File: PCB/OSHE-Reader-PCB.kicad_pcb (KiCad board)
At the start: 2 copper layers, 80 x 100 mm, 76 parts, among them J1 UART, J2 112L-TDA0, J3 JTAG, J5 boot_select, Q1 Si1308EDL, Q2 BSS138, Q3 BSS138, U1 74LVC1G04, U2 TPS923610DRLR, U3 TLV75533PDBV, U4 ESP32-S3-WROOM-1

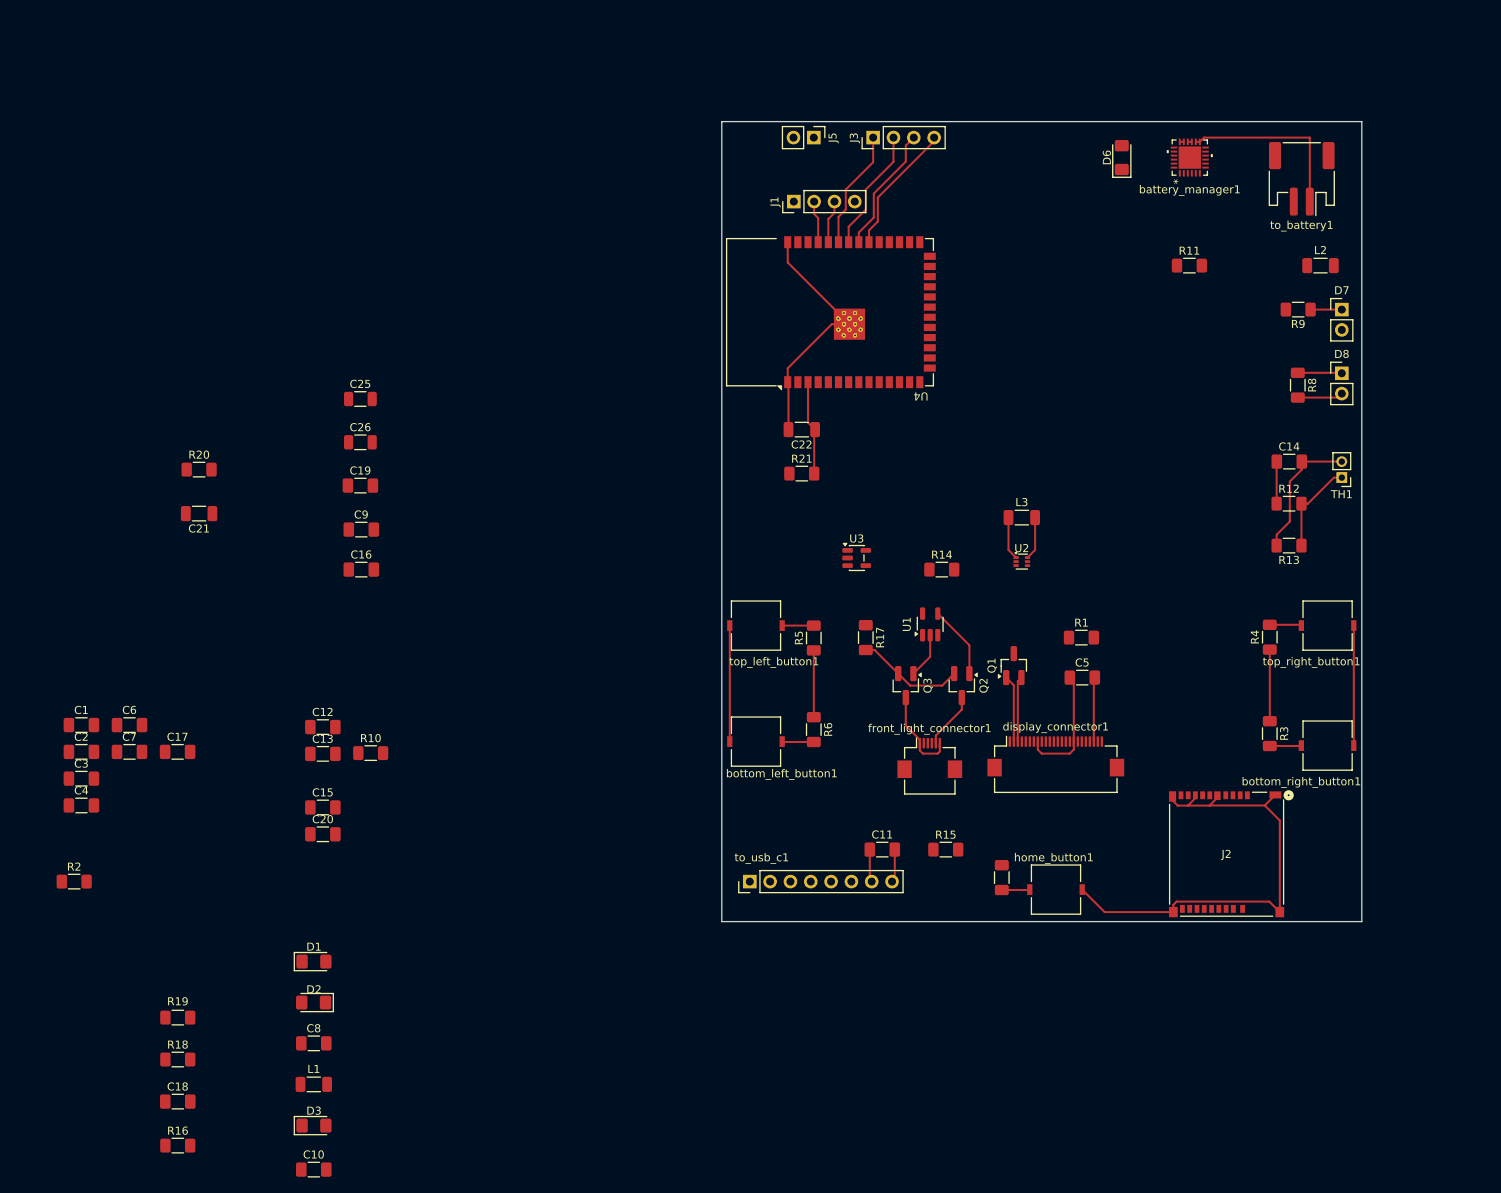
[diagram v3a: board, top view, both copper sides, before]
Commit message: Routed Board
Board is mostly routed except for the left buttons and center button in case they need to get moved. Looked through DRC for a first pass and got most of the errors I think but would appreciate a second set of eyes.
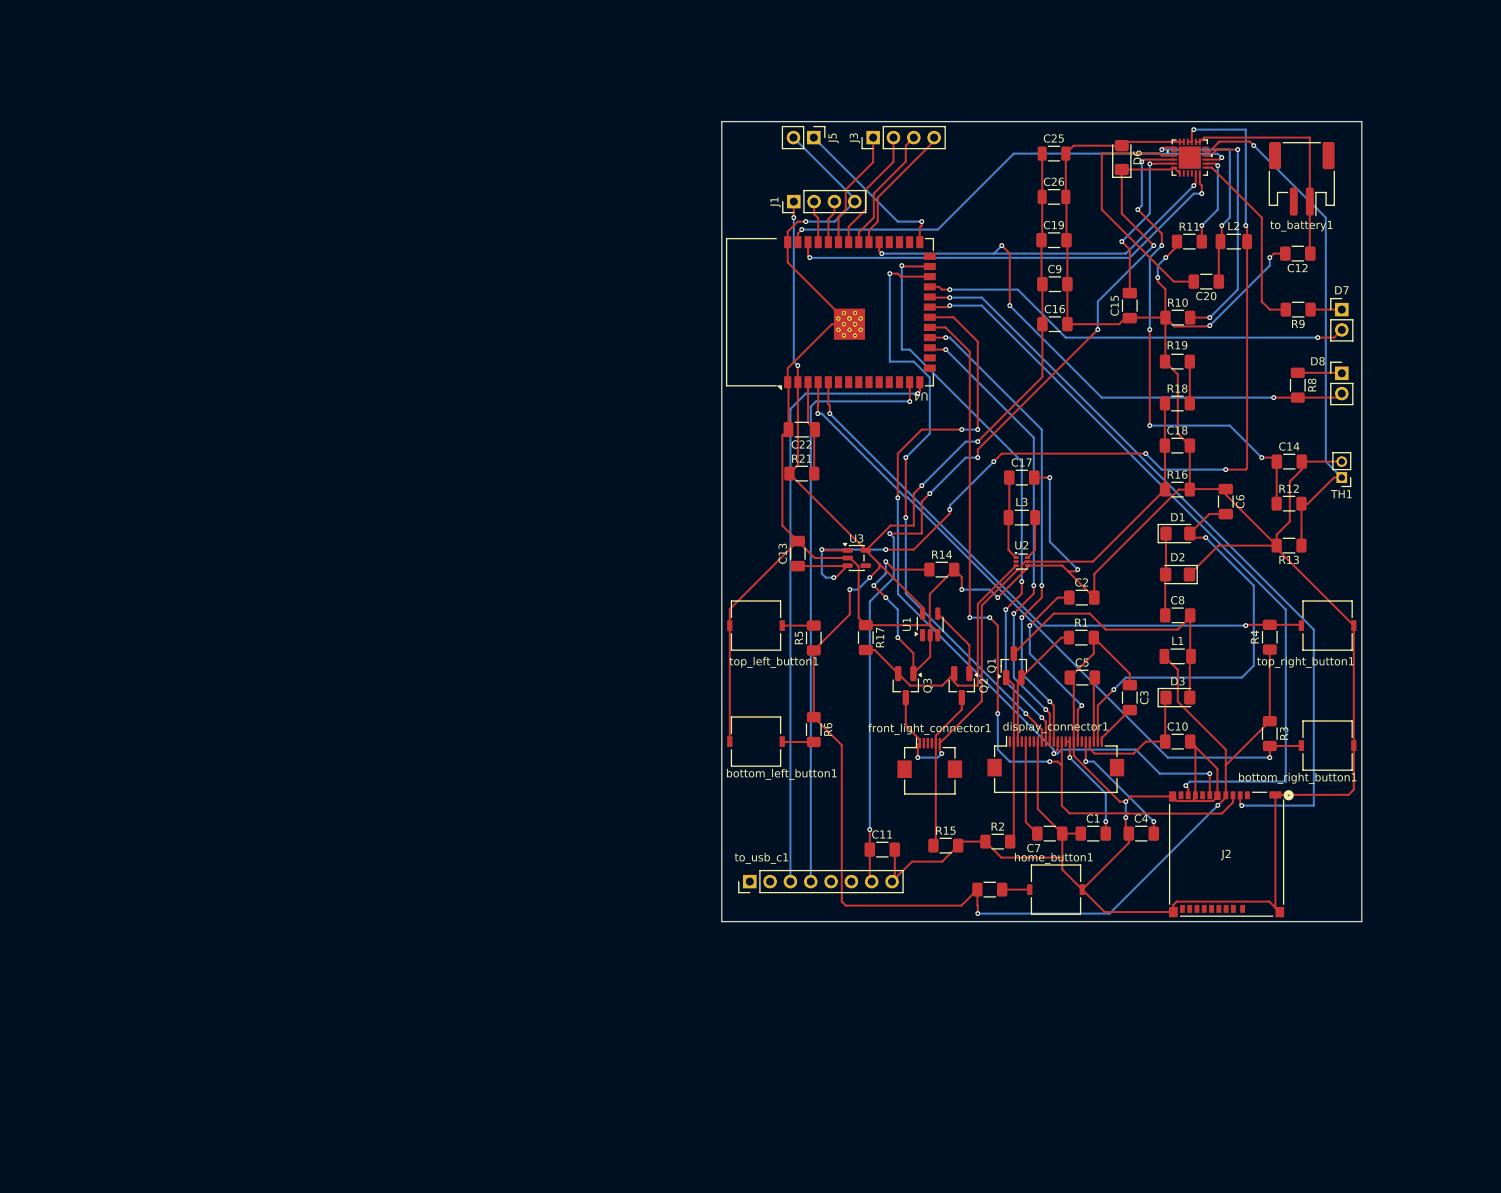
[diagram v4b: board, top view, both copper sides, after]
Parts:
- removed C21: 1uF, Inductor_SMD:L_1206_3216Metric_Pad1.22x1.90mm_HandSolder
- removed R20: 10k, Resistor_SMD:R_1206_3216Metric_Pad1.30x1.75mm_HandSolder
- moved C18 149.5 mm to (170.4, 89.0)
- moved R16 149.5 mm to (170.4, 94.5)
- moved R18 149.5 mm to (170.4, 83.7)
- moved R19 149.5 mm to (170.4, 78.5)
- moved C6 139.9 mm to (176.5, 96.0), turned to -90 degrees
- moved C12 135.5 mm to (185.5, 65.0), turned to 180 degrees
- moved C4 132.5 mm to (165.9, 137.5)
- moved C3 131.4 mm to (164.5, 120.5), turned to -90 degrees
- moved C20 130.3 mm to (174.1, 68.5), turned to 180 degrees
- moved C1 127.2 mm to (159.9, 137.5)
- moved C2 126.5 mm to (158.5, 108.0)
- moved C10 120.5 mm to (170.5, 126.0)
- moved C8 120.5 mm to (170.5, 110.2)
- moved D1 120.5 mm to (170.5, 100.0)
- moved D2 120.5 mm to (170.5, 105.1)
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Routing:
- net GND: track 156.3 -> 551.1 mm, vias 0 -> 11
- net +3V3: track 17.3 -> 263.7 mm, vias 0 -> 8
- net /Battery Charger/SYS: track 0.50 -> 127.2 mm, vias 0 -> 9
- net /VBUS: track 4.10 -> 116.8 mm, vias 0 -> 6
- net /SCL: track 0.00 -> 100.4 mm, vias 0 -> 5
- net /COPI: track 0.00 -> 99.0 mm, vias 0 -> 4
- net /SD_CS: track 0.00 -> 97.6 mm, vias 0 -> 2
- net /CIPO: track 0.00 -> 95.9 mm, vias 0 -> 2
- net /STAT: track 5.71 -> 101.5 mm, vias 0 -> 5
- net /BR_button: track 3.97 -> 83.7 mm, vias 0 -> 2
- net /D+: track 0.00 -> 77.3 mm, vias 0 -> 1
- net /BUSY: track 0.00 -> 75.8 mm, vias 0 -> 4
- net /D-: track 0.00 -> 74.5 mm, vias 0 -> 1
- net /RES_SCR: track 0.00 -> 72.7 mm, vias 0 -> 4
- net /TR_button: track 3.99 -> 74.0 mm, vias 0 -> 2
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
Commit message: pcb
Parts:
- moved C1 49.4 mm to (113.1, 153.0)
- moved C4 49.4 mm to (119.1, 153.0)
- moved C7 49.4 mm to (107.6, 153.0)
- moved R4 45.7 mm to (187.0, 67.5)
- moved R5 45.6 mm to (125.5, 67.5)
- moved top_right_button1 44.2 mm to (193.5, 67.5)
- moved top_left_button1 44.0 mm to (118.5, 67.5), turned to 0 degrees
- moved R13 39.6 mm to (187.0, 62.0), turned to 90 degrees
- moved U3 34.4 mm to (144.1, 71.5)
- moved R12 34.3 mm to (182.5, 62.0), turned to 90 degrees
- moved to_battery1 33.1 mm to (156.8, 39.9)
- moved TH1 32.2 mm to (194.5, 61.0), turned to -90 degrees
- moved battery_manager1 28.6 mm to (160.5, 79.2)
- moved C13 22.9 mm to (145.5, 98.4)
- moved R9 20.2 mm to (165.9, 67.0)
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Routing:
- net GND: track 551.1 -> 0.00 mm, vias 11 -> 0
- net +3V3: track 263.7 -> 0.00 mm, vias 8 -> 0
- net /Battery Charger/SYS: track 127.2 -> 0.00 mm, vias 9 -> 0
- net /VBUS: track 116.8 -> 0.00 mm, vias 6 -> 0
- net /STAT: track 101.5 -> 0.00 mm, vias 5 -> 0
- net /SCL: track 100.4 -> 0.00 mm, vias 5 -> 0
- net /COPI: track 99.0 -> 0.00 mm, vias 4 -> 0
- net /SD_CS: track 97.6 -> 0.00 mm, vias 2 -> 0
- net /CIPO: track 95.9 -> 0.00 mm, vias 2 -> 0
- net /BR_button: track 83.7 -> 0.00 mm, vias 2 -> 0
- net /D+: track 77.3 -> 0.00 mm, vias 1 -> 0
- net /BUSY: track 75.8 -> 0.00 mm, vias 4 -> 0
- net /D-: track 74.5 -> 0.00 mm, vias 1 -> 0
- net /TR_button: track 74.0 -> 0.00 mm, vias 2 -> 0
- net /RES_SCR: track 72.7 -> 0.00 mm, vias 4 -> 0
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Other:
- board size 80 x 100 mm -> 85 x 90 mm
- board text added: "screen"

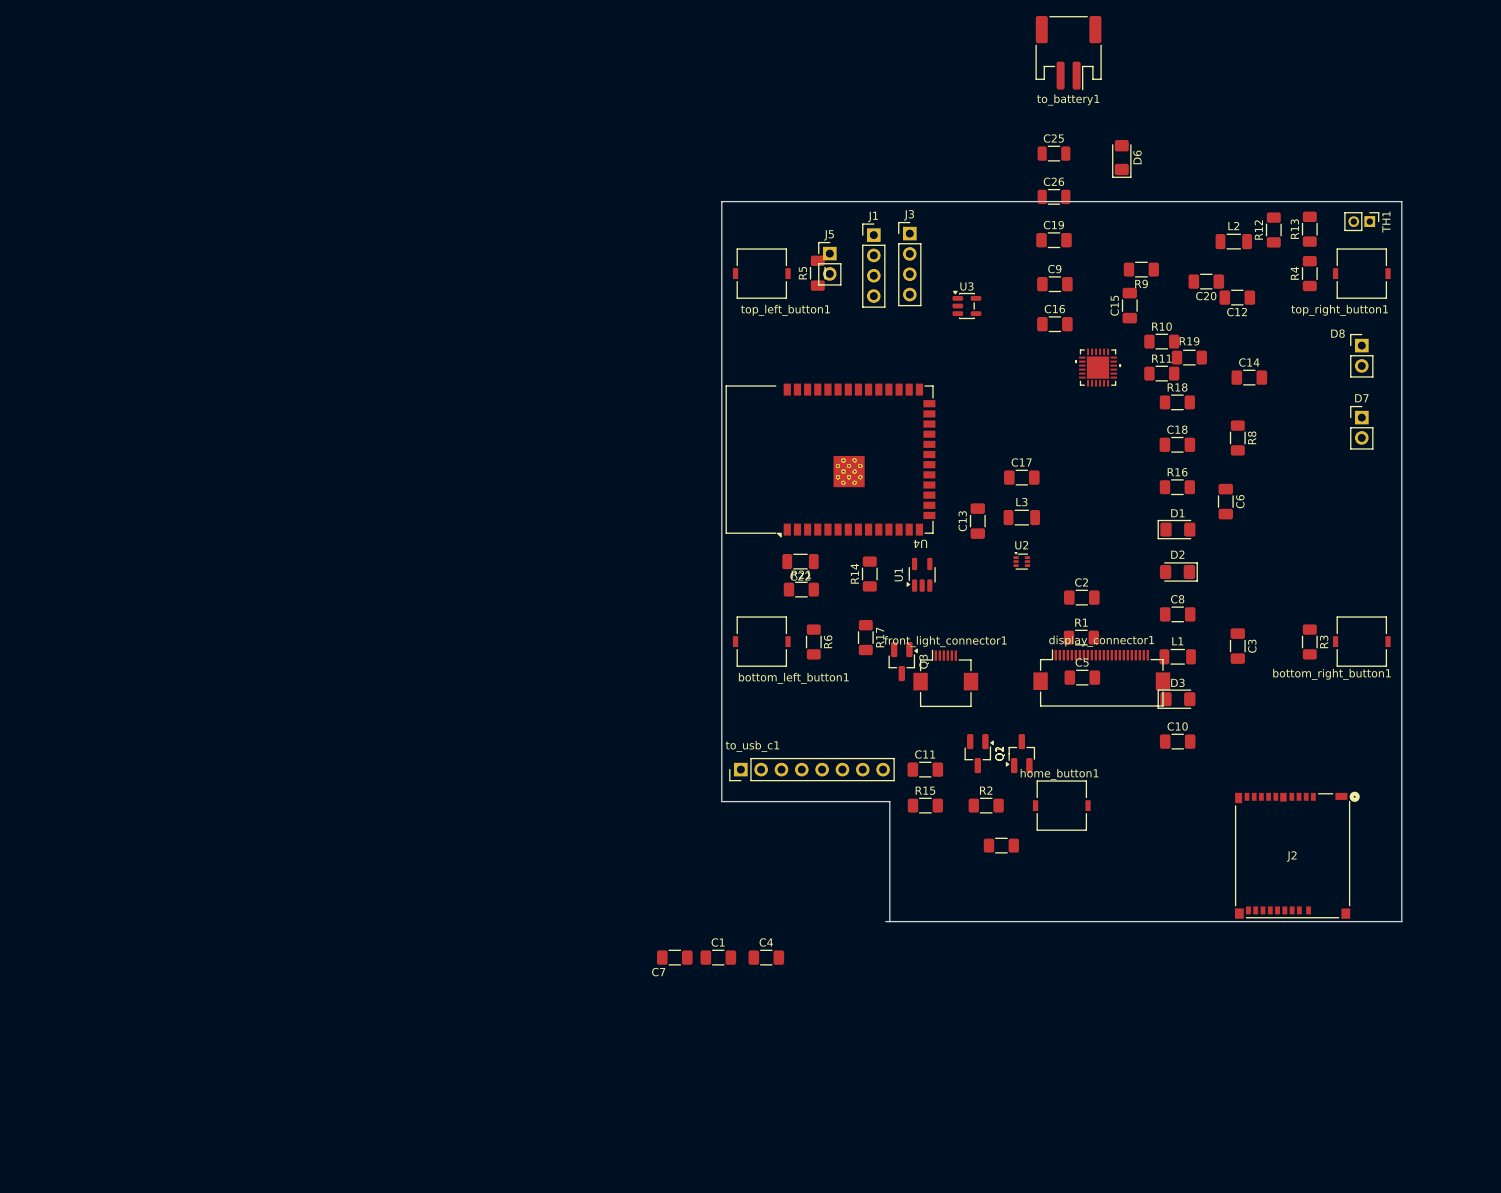
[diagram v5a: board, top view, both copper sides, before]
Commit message: Started Rerouting Board
-Got a gnd plane
-got all components re-organized
-maybe need a 3.3v plane???
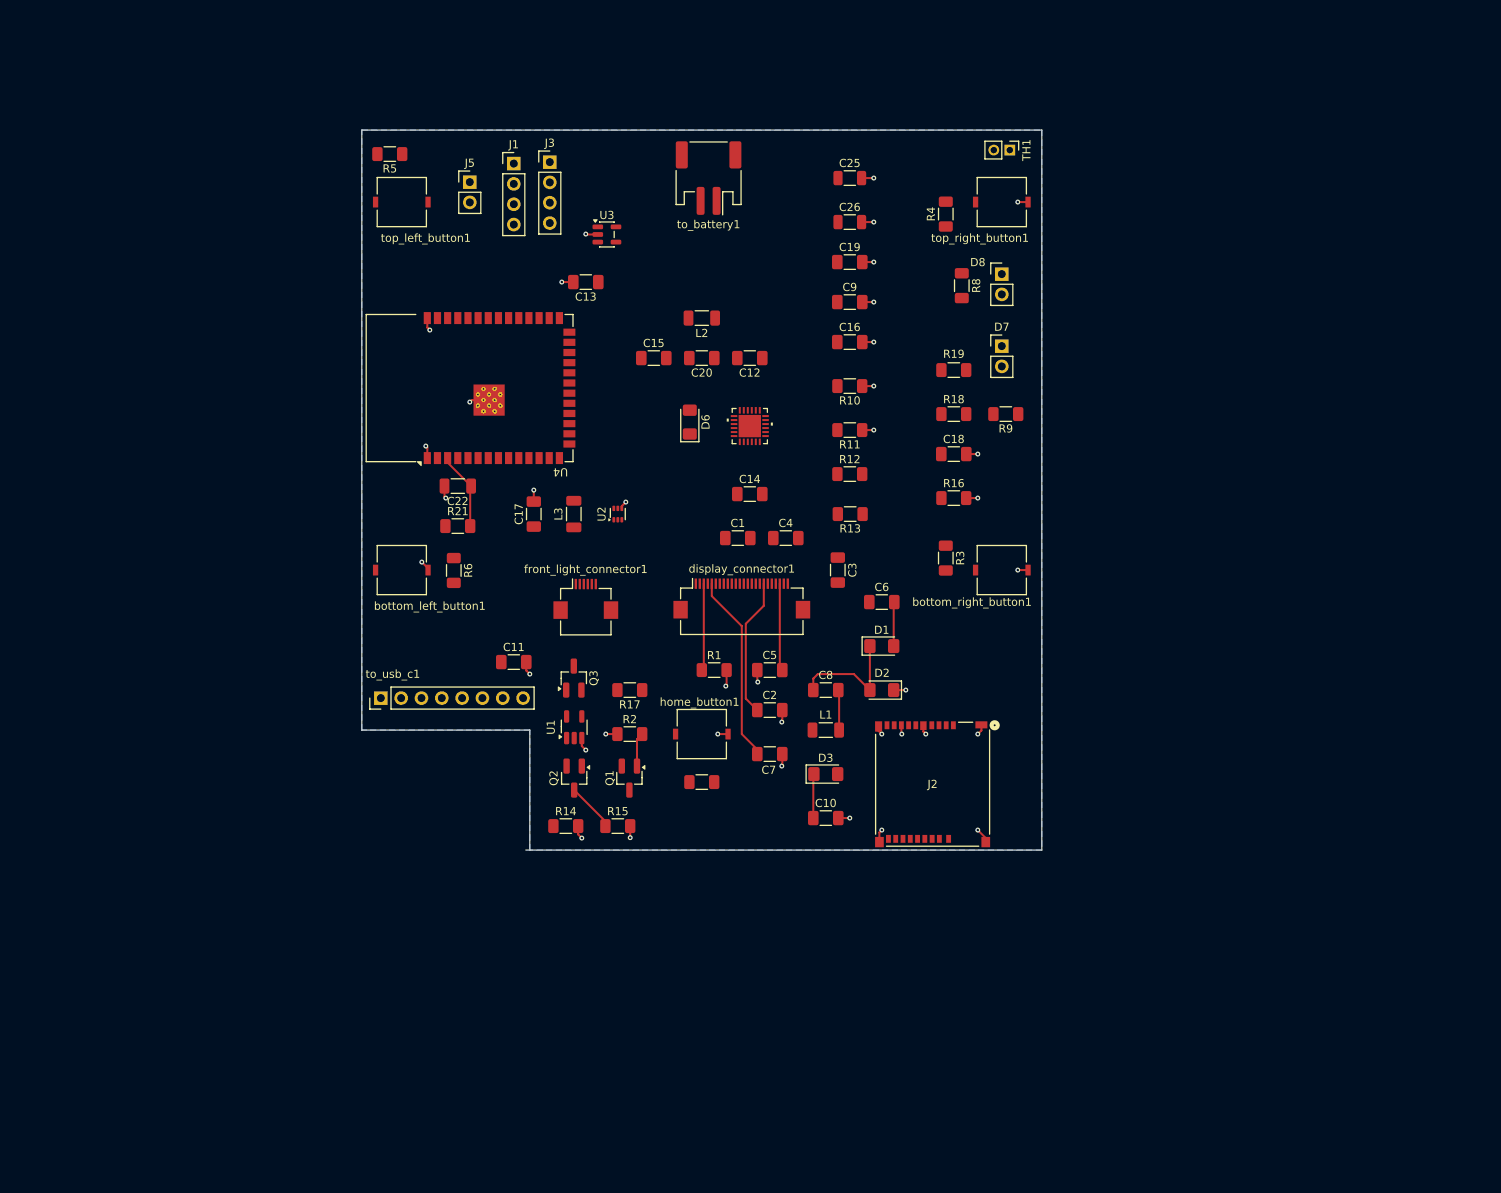
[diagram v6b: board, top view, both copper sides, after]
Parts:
- moved R13 67.6 mm to (129.6, 97.6), turned to 180 degrees
- moved L2 67.2 mm to (111.0, 73.1), turned to 180 degrees
- moved C14 64.1 mm to (117.0, 95.1)
- moved C20 63.8 mm to (111.0, 78.1)
- moved D6 63.3 mm to (109.5, 86.1)
- moved C12 61.4 mm to (117.0, 78.1)
- moved C17 61.2 mm to (90.0, 97.6), turned to 90 degrees
- moved R12 61.2 mm to (129.5, 92.6), turned to 0 degrees
- moved C15 59.9 mm to (105.0, 78.1), turned to 0 degrees
- moved C13 57.4 mm to (96.5, 68.6), turned to 180 degrees
- moved L3 56.0 mm to (95.0, 97.6), turned to 90 degrees
- moved R5 55.5 mm to (72.0, 52.6), turned to 180 degrees
- moved C11 53.2 mm to (87.5, 116.1)
- moved C1 52.5 mm to (115.5, 100.6)
- moved C4 52.5 mm to (121.5, 100.6)
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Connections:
- U4 pad 10: unconnected-(U4-IO17-Pad10) -> /LED_MONIT
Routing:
- net GND: track 0.00 -> 56.8 mm, vias 0 -> 38
- net /Display + Front Light/VSH2: track 0.00 -> 23.7 mm
- net /Display + Front Light/VDD: track 0.00 -> 17.3 mm
- net Net-(D1-K): track 0.00 -> 15.1 mm
- net /Display + Front Light/VSL: track 0.00 -> 10.9 mm
- net /Display + Front Light/RESE: track 0.00 -> 10.9 mm
- net Net-(U4-EN): track 0.00 -> 9.76 mm
- net /Display + Front Light/LED_C-: track 0.00 -> 6.12 mm
- net /Display + Front Light/VGH: track 0.00 -> 5.53 mm
- net /Display + Front Light/VGL: track 0.00 -> 5.53 mm
- net Net-(D3-A): track 0.00 -> 5.04 mm
- net /Display + Front Light/GDR: track 0.00 -> 4.27 mm
- added copper zone on B.Cu, net GND
